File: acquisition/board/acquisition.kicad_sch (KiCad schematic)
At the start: 0 parts

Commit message: Continued initial design
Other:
- added sheet FTDI USB interface (ftdi.kicad_sch)
- sheet ADCs ports: added ADC0_PDWN, ADC1_PDWN, ADC2_PDWN, ADC3_PDWN, PLL_UWIRE_CLK, PLL_UWIRE_DATA, PLL_UWIRE_LE, SYNC_OUT, SYS_CLK_N, SYS_CLK_P; removed none
- sheet Clocking ports: added 3V3, CLK_4, CLK_5_N, CLK_5_P, GND, PLL_STATUS_CLKIN0, PLL_STATUS_CLKIN1, PLL_STATUS_HOLDOVER, PLL_STATUS_LD, PLL_SYNC, UWIRE_CLK, UWIRE_DATA, UWIRE_LE; removed SYNC_0, SYNC_1, SYNC_2, SYNC_3
- sheet FPGA support ports: added 1V2, 2V5, 3V3, FPGA_DONE, FPGA_INIT_B, FPGA_RST_N; removed none
- sheet MCU ports: added ADC0_PDWN, ADC1_PDWN, ADC2_PDWN, ADC3_PDWN, D1V8, FPGA_DONE, FPGA_INIT_B, FPGA_RST_N, GND, MCU_SPI_CS_N, MCU_SPI_SCK, MCU_SPI_SI, MCU_SPI_SO, PLL_STATUS_CLKIN0, PLL_STATUS_CLKIN1, PLL_STATUS_HOLDOVER, PLL_STATUS_LD, PLL_SYNC; removed none
- sheet Power Supply ports: added 1V0, 2V5, 3V3, A1V8, D1V8, GND, VREF; removed none
- sheet RAM ports: added MCU_SPI_CS_N, MCU_SPI_SCK, MCU_SPI_SI, MCU_SPI_SO; removed none

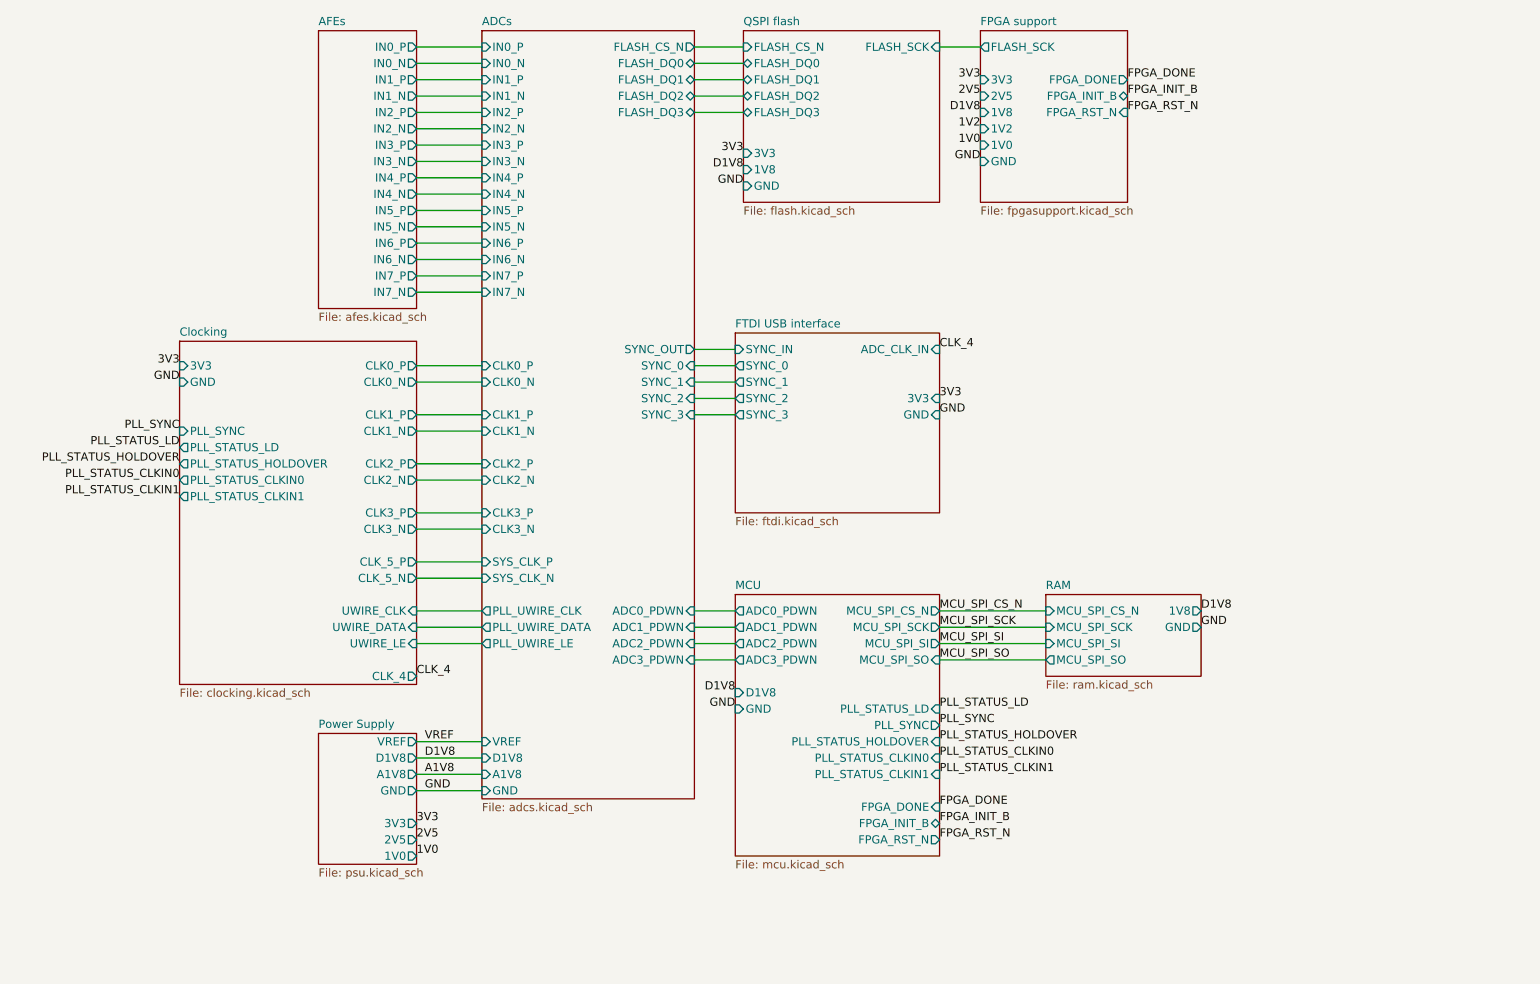
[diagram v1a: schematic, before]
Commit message: Updated schematic with a lot of level shifting and support stuff, power decoupling, etc. Almost done except power supply and protection diodes
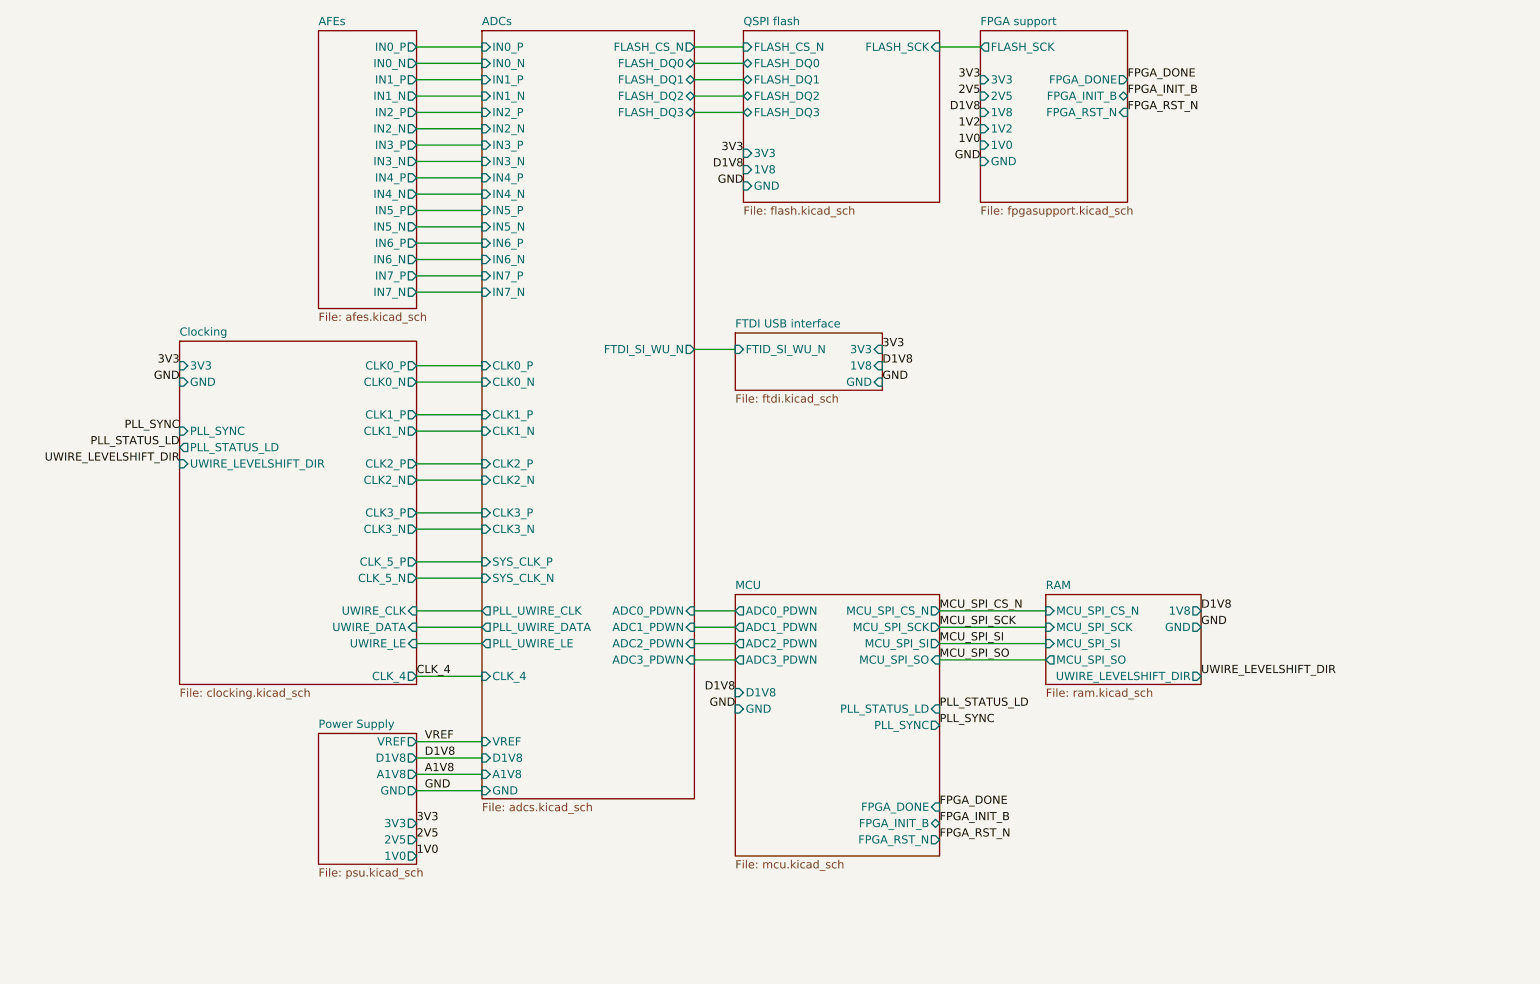
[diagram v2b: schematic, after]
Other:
- sheet ADCs ports: added CLK_4, FTDI_SI_WU_N; removed SYNC_0, SYNC_1, SYNC_2, SYNC_3, SYNC_OUT
- sheet Clocking ports: added UWIRE_LEVELSHIFT_DIR; removed PLL_STATUS_CLKIN0, PLL_STATUS_CLKIN1, PLL_STATUS_HOLDOVER
- sheet FTDI USB interface ports: added 1V8, FTID_SI_WU_N; removed ADC_CLK_IN, SYNC_0, SYNC_1, SYNC_2, SYNC_3, SYNC_IN
- sheet MCU ports: added none; removed PLL_STATUS_CLKIN0, PLL_STATUS_CLKIN1, PLL_STATUS_HOLDOVER
- sheet RAM ports: added UWIRE_LEVELSHIFT_DIR; removed none

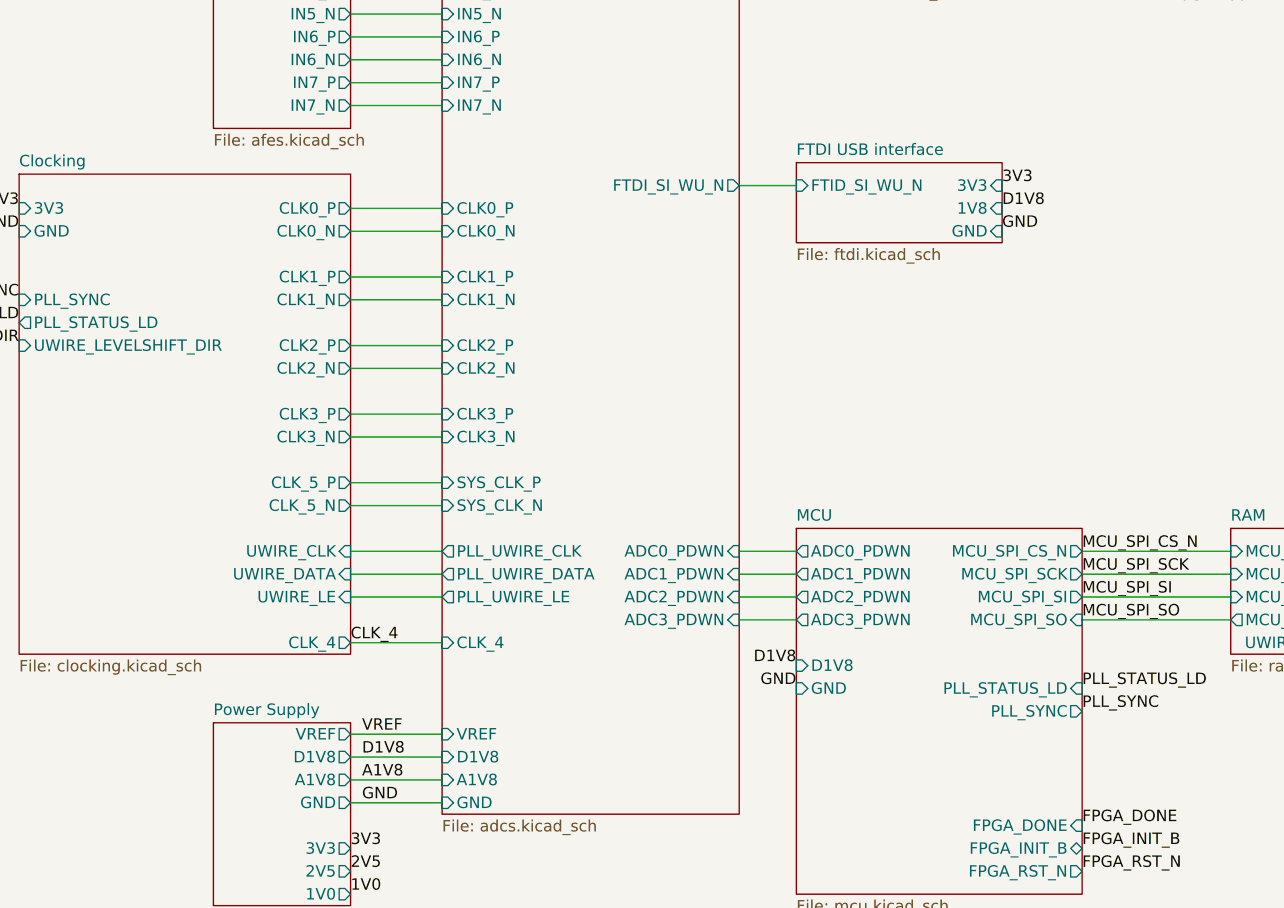
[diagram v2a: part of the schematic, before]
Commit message: Lots of progress on power supply design, added a bunch of test points, etc
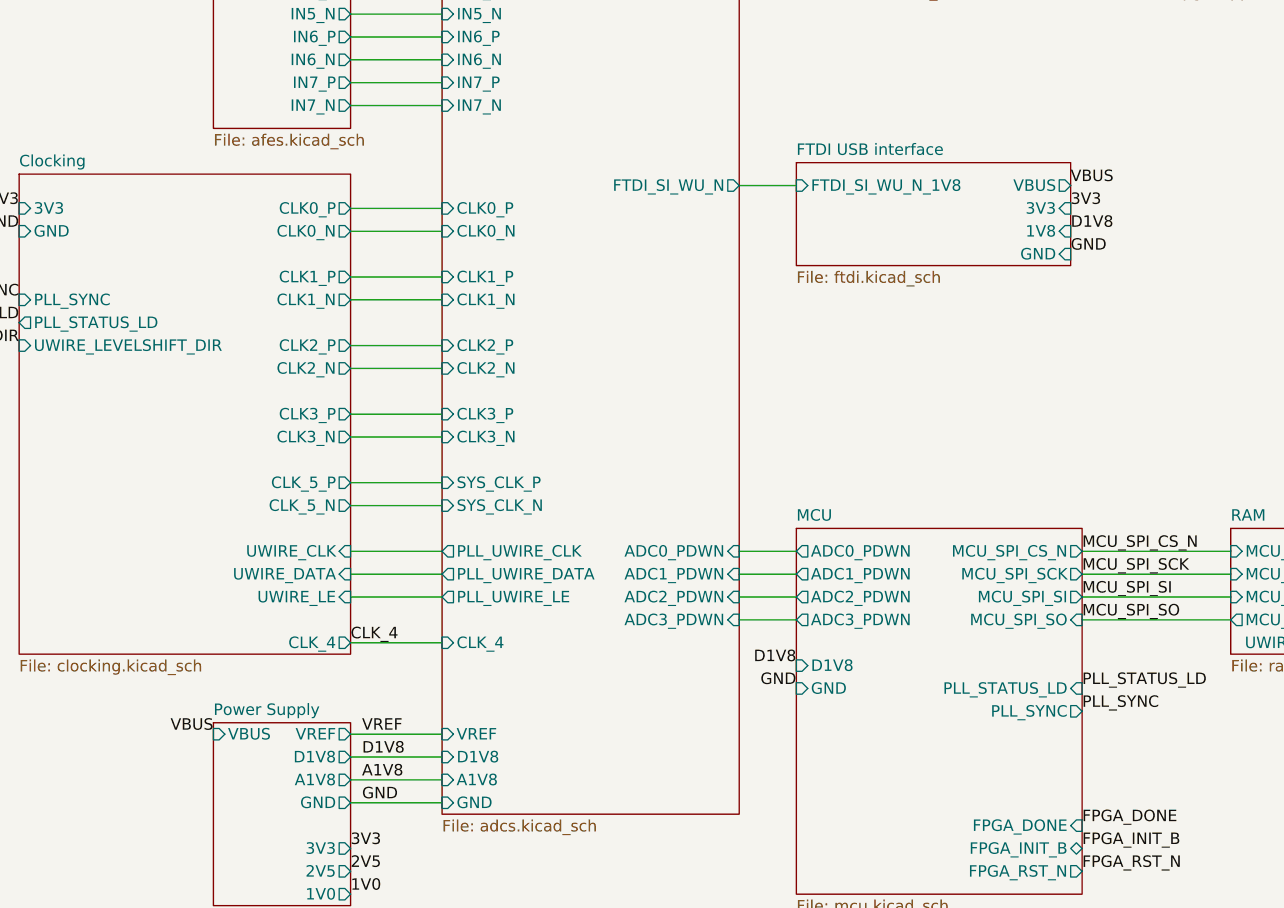
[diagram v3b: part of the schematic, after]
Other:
- sheet FTDI USB interface ports: added FTDI_SI_WU_N_1V8, VBUS; removed FTID_SI_WU_N
- sheet Power Supply ports: added VBUS; removed none

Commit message: More power supply work, added PLL loop filter, soft start, began assigning footprints
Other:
- sheet ADCs ports: added A1V8_1, A1V8_2; removed A1V8
- sheet AFEs ports: added GND; removed none
- sheet Clocking ports: added 1V8; removed none
- sheet MCU ports: added 3V3, VTEMP; removed none
- sheet Power Supply ports: added 1V2, A1V8_1, A1V8_2, LTC_TEMP; removed A1V8

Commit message: Continued layout of bottom ADC, routed FPGA JTAG
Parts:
- added MH1, MH2, MH3, MH4: HOLE_4x40, azonenberg_pcb:MECHANICAL_CLEARANCEHOLE_4_40, symbol conn:CONN_01X01
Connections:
- no-connect marks 0 -> 4
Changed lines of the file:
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@@
   (title_block
     (title "Digitizer board")
-    (date "2023-01-29")
+    (date "2023-01-31")
     (rev "0.1")
     (company "A. Zonenberg")
   )
+  (no_connect (at 236.22 29.21))
+  (no_connect (at 236.22 35.56))
+  (no_connect (at 236.22 41.91))
+  (no_connect (at 236.22 48.26))
   (wire (pts (xy 82.55 57.15) (xy 92.71 57.15))
     (stroke (width 0) (type default) (color 0 0 0 0))
@@
   (label "2V5" (at 82.55 149.86 0)
     (effects (font (size 1.27 1.27)) (justify left bottom))
+  )
+  (symbol (lib_id "conn:CONN_01X01") (at 241.3 41.91 0) (unit 1)
+    (in_bom yes) (on_board yes) (fields_autoplaced)
+    (property "Reference" "MH3" (id 0) (at 243.205 41.0015 0)
+      (effects (font (size 1.27 1.27)) (justify left))
+    )
+    (property "Value" "HOLE_4x40" (id 1) (at 243.205 43.7766 0)
+      (effects (font (size 1.27 1.27)) (justify left))
+    )
+    (property "Footprint" "azonenberg_pcb:MECHANICAL_CLEARANCEHOLE_4_40" (id 2) (at 241.3 41.91 0)
+      (effects (font (size 1.27 1.27)) hide)
+    )
+    (property "Datasheet" "" (id 3) (at 241.3 41.91 0)
+      (effects (font (size 1.27 1.27)) hide)
+    )
+    (pin "1")
+  )
+  (symbol (lib_id "conn:CONN_01X01") (at 241.3 35.56 0) (unit 1)
+    (in_bom yes) (on_board yes) (fields_autoplaced)
+    (property "Reference" "MH2" (id 0) (at 243.205 34.6515 0)
+      (effects (font (size 1.27 1.27)) (justify left))
+    )
+    (property "Value" "HOLE_4x40" (id 1) (at 243.205 37.4266 0)
+      (effects (font (size 1.27 1.27)) (justify left))
+    )
+    (property "Footprint" "azonenberg_pcb:MECHANICAL_CLEARANCEHOLE_4_40" (id 2) (at 241.3 35.56 0)
+      (effects (font (size 1.27 1.27)) hide)
+    )
+    (property "Datasheet" "" (id 3) (at 241.3 35.56 0)
+      (effects (font (size 1.27 1.27)) hide)
+    )
+    (pin "1")
+  )
+  (symbol (lib_id "conn:CONN_01X01") (at 241.3 48.26 0) (unit 1)
+    (in_bom yes) (on_board yes) (fields_autoplaced)
+    (property "Reference" "MH4" (id 0) (at 243.205 47.3515 0)
+      (effects (font (size 1.27 1.27)) (justify left))
+    )
+    (property "Value" "HOLE_4x40" (id 1) (at 243.205 50.1266 0)
+      (effects (font (size 1.27 1.27)) (justify left))
+    )
+    (property "Footprint" "azonenberg_pcb:MECHANICAL_CLEARANCEHOLE_4_40" (id 2) (at 241.3 48.26 0)
+      (effects (font (size 1.27 1.27)) hide)
+    )
+    (property "Datasheet" "" (id 3) (at 241.3 48.26 0)
+      (effects (font (size 1.27 1.27)) hide)
+    )
+    (pin "1")
+  )
+  (symbol (lib_id "conn:CONN_01X01") (at 241.3 29.21 0) (unit 1)
+    (in_bom yes) (on_board yes) (fields_autoplaced)
+    (property "Reference" "MH1" (id 0) (at 243.205 28.3015 0)
+      (effects (font (size 1.27 1.27)) (justify left))
+    )
+    (property "Value" "HOLE_4x40" (id 1) (at 243.205 31.0766 0)
+      (effects (font (size 1.27 1.27)) (justify left))
+    )
+    (property "Footprint" "azonenberg_pcb:MECHANICAL_CLEARANCEHOLE_4_40" (id 2) (at 241.3 29.21 0)
+      (effects (font (size 1.27 1.27)) hide)
+    )
+    (property "Datasheet" "" (id 3) (at 241.3 29.21 0)
+      (effects (font (size 1.27 1.27)) hide)
+    )
+    (pin "1")
   )
   (sheet (at 67.31 130.81) (size 15.24 30.48) (fields_autoplaced)
@@
       (reference "L9") (unit 1) (value "NRS5030T2R2NMGJ") (footprint "azonenberg_pcb:INDUCTOR_YUDEN_NRS5030")
     )
+    (path "/d8c254c1-6213-4cf2-b6ac-ebd03c35f2e2"
+      (reference "MH1") (unit 1) (value "HOLE_4x40") (footprint "azonenberg_pcb:MECHANICAL_CLEARANCEHOLE_4_40")
+    )
+    (path "/b7264511-870b-410e-85ec-27b54d33e749"
+      (reference "MH2") (unit 1) (value "HOLE_4x40") (footprint "azonenberg_pcb:MECHANICAL_CLEARANCEHOLE_4_40")
+    )
+    (path "/55a5ba65-eb02-4fd3-bd69-7999adff3737"
+      (reference "MH3") (unit 1) (value "HOLE_4x40") (footprint "azonenberg_pcb:MECHANICAL_CLEARANCEHOLE_4_40")
+    )
+    (path "/bb4efe53-87a7-4d03-bfc7-e242965fd927"
+      (reference "MH4") (unit 1) (value "HOLE_4x40") (footprint "azonenberg_pcb:MECHANICAL_CLEARANCEHOLE_4_40")
+    )
     (path "/3080725e-4daa-400d-bea8-e04c3293c784/b3038db0-aa78-49a5-923e-1f947c7f9305"
